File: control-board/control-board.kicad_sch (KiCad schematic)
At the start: 85 parts, among them J1 Conn_01x03, J10 DIN-4, J11 DIN-4, J2 GPS_ANT, J3 LORA_ANT, J4 DIN-4, J5 DIN-4, J6 USB_C_Receptacle_USB2.0_16P, J7 DIN-4, J8 DIN-4, J9 DIN-4, Q1 2N7002, SW1 SW_SPST, U1 STM32H743VITx, U2 NEO-XM, U3 SN65HVD256D, U4 AMS1117-3.3, U5 AP63200WU, U6 AMS1117-3.3, U7 SN65HVD256D, Y1 8M, Y2 32.768k

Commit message: control-board: update Ver 2025.9-1
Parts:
- added D3, D4, D5, D6: LED, LED_SMD:LED_0805_2012Metric, symbol Device:LED
- added H1, H2, H3, H4: MountingHole_Pad, MountingHole:MountingHole_3.2mm_M3_ISO14580_Pad, symbol Mechanical:MountingHole_Pad
- added J12, J13: Conn_01x03, Connector_PinHeader_2.54mm:PinHeader_1x03_P2.54mm_Vertical, symbol Connector_Generic:Conn_01x03
- J10, J11, J4, J5, J7, J8, J9: footprint (none) -> M8_conn_panel:M8_Female_Conn_Panel_P4_90
- JP1, JP2: footprint PCM_Jumper_AKL:Jumper_P2.54mm_D1.2mm -> Connector_PinHeader_2.54mm:PinHeader_1x02_P2.54mm_Vertical
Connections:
- net GND: now also D3.1 (K), D4.1 (K), D5.1 (K), D6.1 (K), H1.1, H2.1, H3.1, H4.1; no longer R15.2, R16.2, R17.2, R9.2
- net GPIO1: now reaches U1.57 (PD10)
- net GPIO1: now also J12.1 (Pin_1)
- net GPIO2: now reaches U1.58 (PD11)
- net GPIO2: now also J12.2 (Pin_2)
- net GPIO3: now reaches U1.59 (PD12)
- net GPIO3: now also J12.3 (Pin_3)
- net GPIO4: now reaches U1.60 (PD13)
- net GPIO4: now also J13.1 (Pin_1)
- net GPIO5: now reaches U1.61 (PD14)
- net GPIO5: now also J13.2 (Pin_2)
- net GPIO6: now reaches U1.62 (PD15)
- net GPIO6: now also J13.3 (Pin_3)
- net GPIO7: now reaches U1.83 (PD2)
- net GPIO8: now reaches U1.84 (PD3)
- net GPIO9: now reaches U1.85 (PD4)
- new net: D3.2 (A), R15.2
- new net: D6.2 (A), R9.2
- new net: D4.2 (A), R16.2
- new net: D5.2 (A), R17.2
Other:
- moved on the sheet: R15, R16, R17, R9

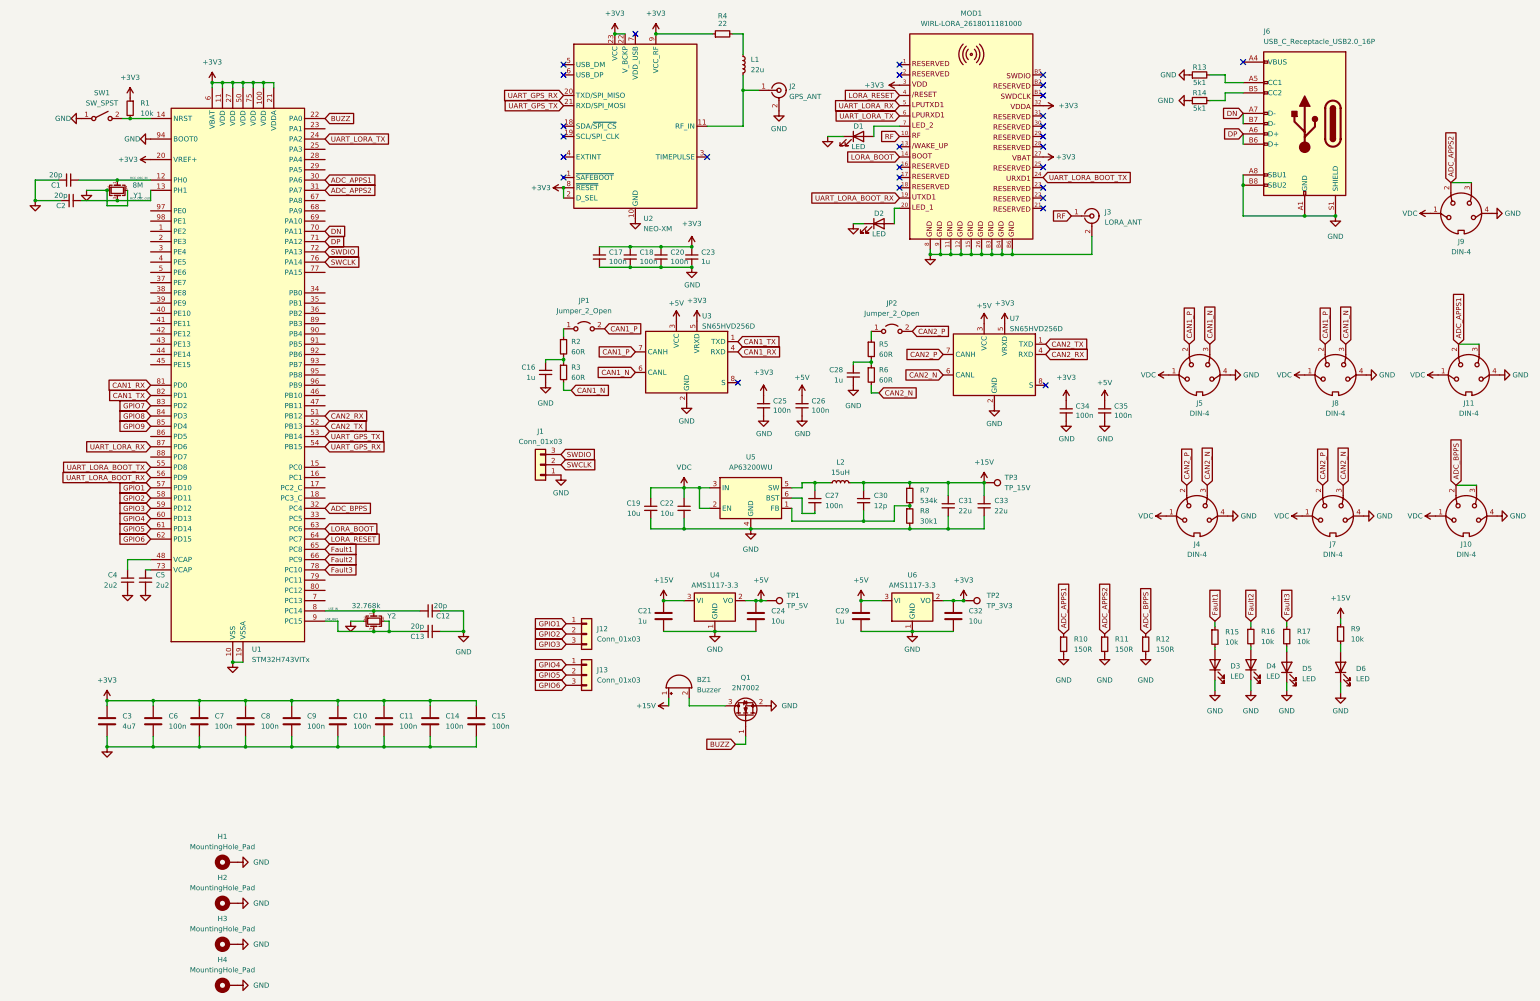
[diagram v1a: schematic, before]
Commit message: modify: control board schematic
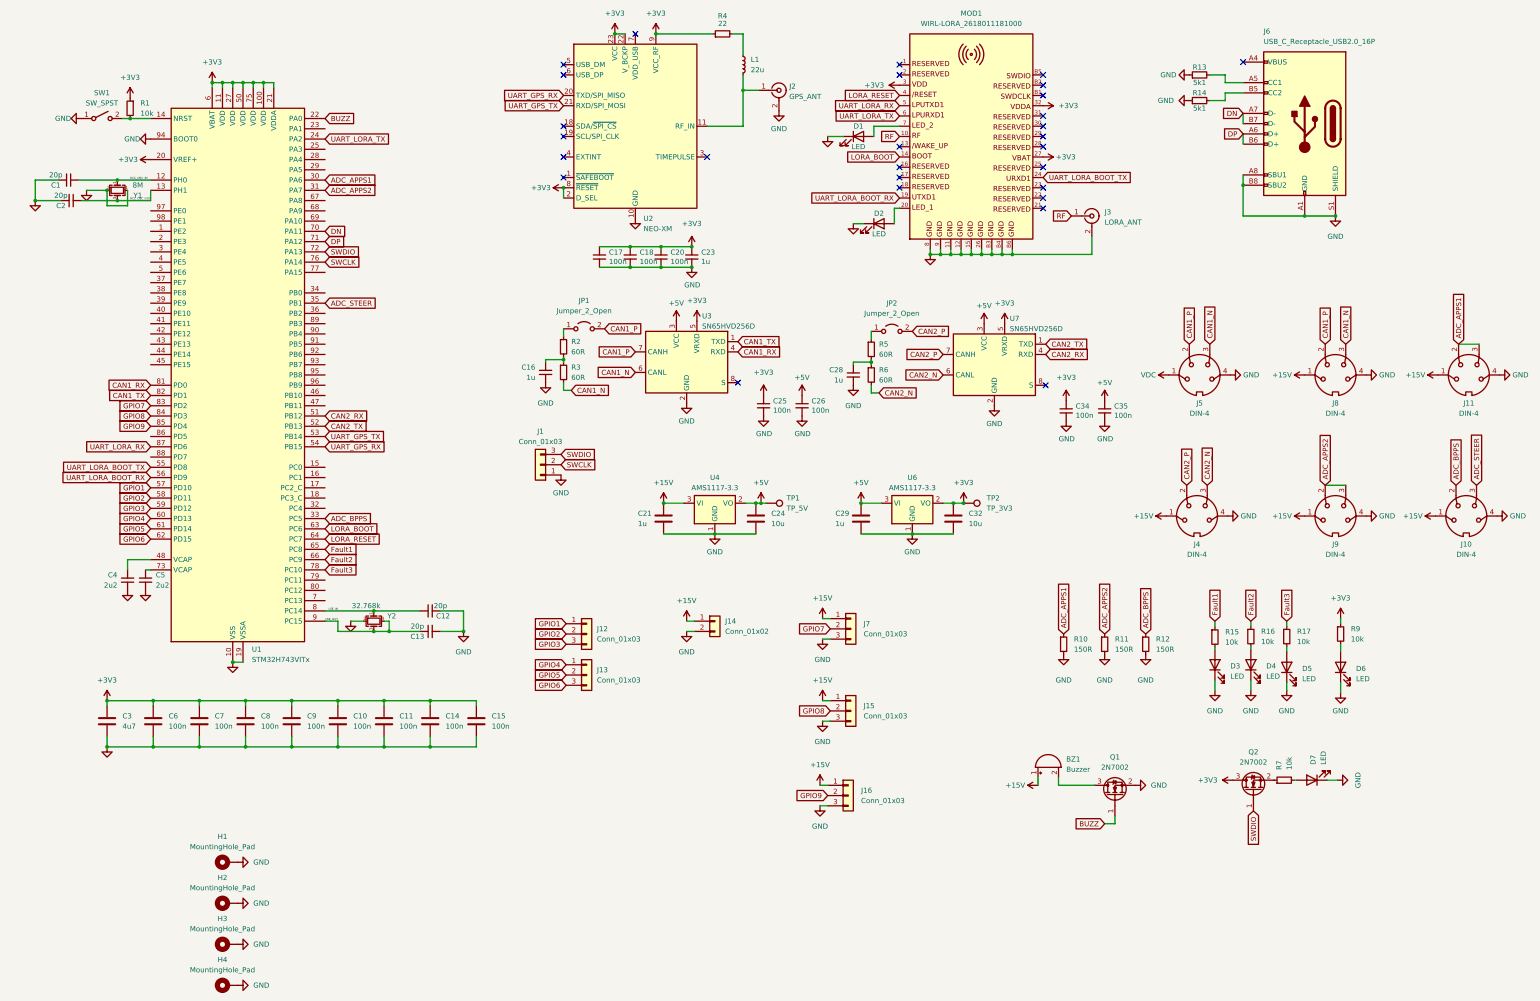
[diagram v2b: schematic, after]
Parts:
- removed C19, C22: 10u, Capacitor_SMD:C_0805_2012Metric, symbol Device:C_Small
- removed C27: 100n, Capacitor_SMD:C_0603_1608Metric, symbol Device:C_Small
- removed C30: 12p, Capacitor_SMD:C_0603_1608Metric, symbol Device:C_Small
- removed C31, C33: 22u, Capacitor_SMD:C_0805_2012Metric, symbol Device:C_Small
- removed J7: DIN-4, M8_conn_panel:M8_Female_Conn_Panel_P4_90, symbol Connector:DIN-4
- removed L2: 15uH, Inductor_SMD:L_Coilcraft_XAL6060-XXX, symbol Device:L_Small
- removed R8: 30k1, Resistor_SMD:R_0603_1608Metric, symbol Device:R_Small
- removed TP3: TP_15V, TestPoint:TestPoint_THTPad_D1.5mm_Drill0.7mm, symbol Connector:TestPoint
- removed U5: AP63200WU, Package_TO_SOT_SMD:TSOT-23-6, symbol Regulator_Switching:AP63200WU
- added D7: LED, LED_SMD:LED_0805_2012Metric, symbol Device:LED
- added J14: Conn_01x02, Connector_PinHeader_2.54mm:PinHeader_1x02_P2.54mm_Vertical, symbol Connector_Generic:Conn_01x02
- added J15, J16, J7: Conn_01x03, symbol Connector_Generic:Conn_01x03
- added Q2: 2N7002, Package_TO_SOT_SMD:SOT-23, symbol Transistor_FET:2N7002
- R7: value 534k -> 10k
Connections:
- net +15V: now also J10.1, J11.1, J4.1, J8.1, J9.1, J14.1 (Pin_1), J15.1 (Pin_1), J16.1 (Pin_1), J7.1 (Pin_1); no longer R7.1, R9.1
- net +3V3: now also R9.1, Q2.3 (D)
- net ADC_BPPS: now also U1.33 (PC5); no longer J10.3, U1.32 (PC4)
- net GND: now also D7.1 (K), J14.2 (Pin_2), J15.3 (Pin_3), J16.3 (Pin_3), J7.3 (Pin_3)
- net GPIO7: now also J7.2 (Pin_2)
- net GPIO8: now also J15.2 (Pin_2)
- net GPIO9: now also J16.2 (Pin_2)
- net SWDIO: now also Q2.1 (G)
- net VDC: no longer J10.1, J11.1, J4.1, J8.1, J9.1
- net at R7.2: now also D7.2 (A)
- net ADC_STEER: now reaches U1.35 (PB1)
- net ADC_STEER: now also J10.3
- new net: Q2.2 (S), R7.1
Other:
- moved on the sheet: BZ1, C21, C24, C29, C32, J9, Q1, TP1, TP2, U4, U6

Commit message: modify: control board
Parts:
- removed J16: Conn_01x03, symbol Connector_Generic:Conn_01x03
- added D8: BAT46, Diode_THT:D_DO-35_SOD27_P7.62mm_Horizontal, symbol Diode:BAT46
- J15, J7: footprint (none) -> Connector_JST:JST_EH_B3B-EH-A_1x03_P2.50mm_Vertical
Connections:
- net +15V: no longer J8.1
- net +3V3: now also R7.1; no longer Q2.3 (D)
- net +5V: now also D8.1 (K)
- net GND: now also Q2.2 (S); no longer D7.1 (K)
- net VDC: now also J8.1
- net at J6.A4 (VBUS), J6.A9 (VBUS), J6.B4 (VBUS)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: now also D8.2 (A)
- net GPIO9: no longer names the net of U1.85 (PD4)
- new net: D7.1 (K), Q2.3 (D)
- no-connect marks 28 -> 27
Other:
- moved on the sheet: D7, Q2, R13, R14, R7

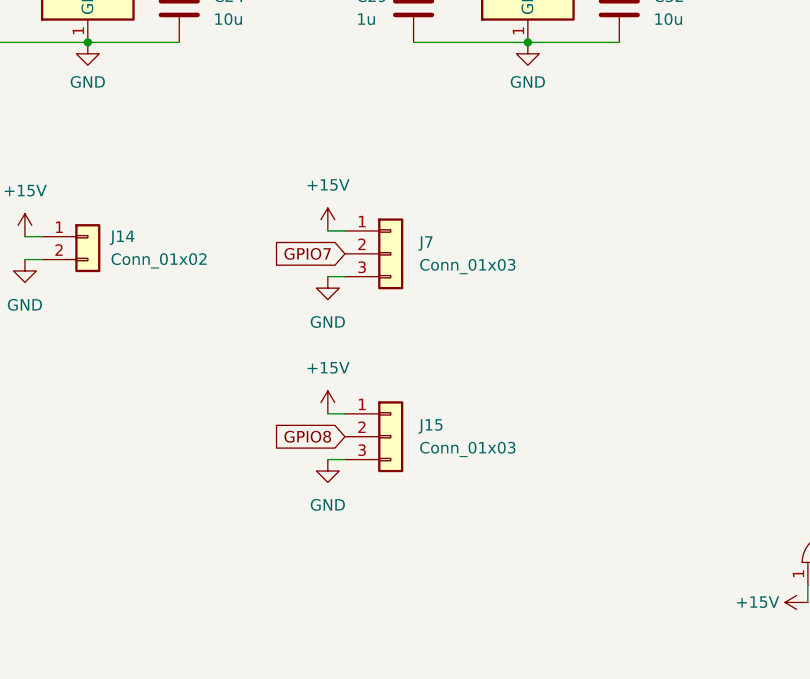
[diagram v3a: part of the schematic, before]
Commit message: modify: diodes and JST footprint
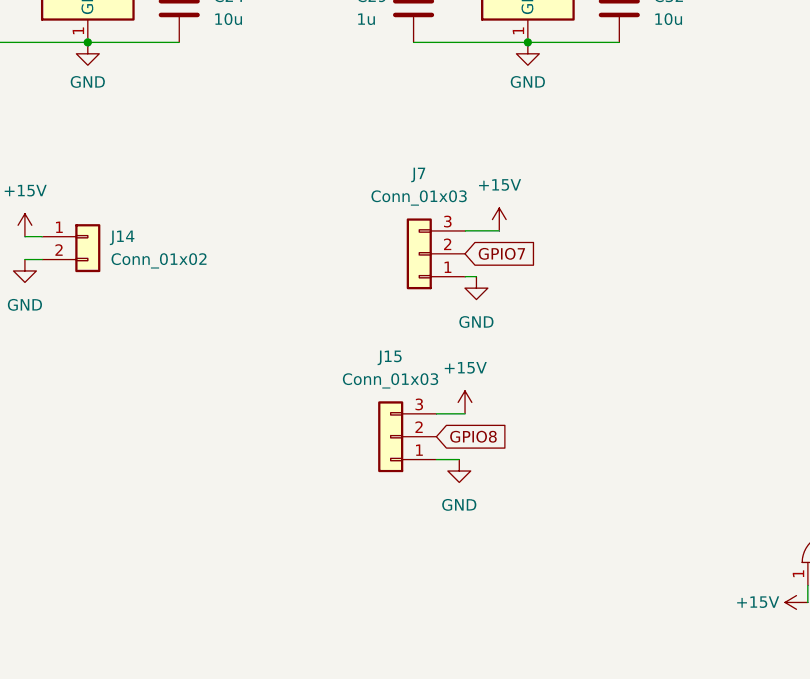
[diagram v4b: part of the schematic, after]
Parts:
- D8: footprint Diode_THT:D_DO-35_SOD27_P7.62mm_Horizontal -> Diode_SMD:D_SOD-123
- J15, J7: footprint Connector_JST:JST_EH_B3B-EH-A_1x03_P2.50mm_Vertical -> Connector_JST:JST_XH_B3B-XH-A_1x03_P2.50mm_Vertical
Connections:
- net +15V: now also J15.3 (Pin_3), J7.3 (Pin_3); no longer J15.1 (Pin_1), J7.1 (Pin_1)
- net GND: now also J15.1 (Pin_1), J7.1 (Pin_1); no longer J15.3 (Pin_3), J7.3 (Pin_3)
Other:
- moved on the sheet: J15, J7
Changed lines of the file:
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@@
     (stroke (width 0) (type default))
   )
+  (wire (pts (xy 241.935 171.45) (xy 240.665 171.45))
+    (stroke (width 0) (type default))
+  )
   (wire (pts (xy 48.26 186.69) (xy 59.69 186.69))
     (stroke (width 0) (type default))
@@
     (stroke (width 0) (type default))
   )
+  (wire (pts (xy 237.49 186.69) (xy 240.665 186.69))
+    (stroke (width 0) (type default))
+  )
   (wire (pts (xy 283.845 205.74) (xy 283.845 207.645))
     (stroke (width 0) (type default))
@@
     (stroke (width 0) (type default))
   )
-  (wire (pts (xy 225.425 191.77) (xy 227.33 191.77))
-    (stroke (width 0) (type default))
-  )
   (wire (pts (xy 53.34 60.325) (xy 53.34 64.135))
     (stroke (width 0) (type default))
@@
     (stroke (width 0) (type default))
   )
-  (wire (pts (xy 225.425 186.69) (xy 227.33 186.69))
-    (stroke (width 0) (type default))
-  )
   (wire (pts (xy 234.95 145.415) (xy 247.65 145.415))
     (stroke (width 0) (type default))
@@
     (stroke (width 0) (type default))
   )
+  (wire (pts (xy 240.03 191.77) (xy 237.49 191.77))
+    (stroke (width 0) (type default))
+  )
   (wire (pts (xy 292.1 76.2) (xy 292.1 71.755))
     (stroke (width 0) (type default))
@@
     (stroke (width 0) (type default))
   )
-  (wire (pts (xy 225.425 171.45) (xy 227.33 171.45))
-    (stroke (width 0) (type default))
-  )
   (wire (pts (xy 272.415 76.2) (xy 292.1 76.2))
     (stroke (width 0) (type default))
@@
     (stroke (width 0) (type default))
   )
-  (wire (pts (xy 82.55 198.12) (xy 93.98 198.12))
+  (wire (pts (xy 244.475 166.37) (xy 240.665 166.37))
     (stroke (width 0) (type default))
   )
-  (wire (pts (xy 30.48 62.865) (xy 30.48 57.785))
+  (wire (pts (xy 82.55 198.12) (xy 93.98 198.12))
     (stroke (width 0) (type default))
   )
-  (wire (pts (xy 225.425 166.37) (xy 227.33 166.37))
+  (wire (pts (xy 30.48 62.865) (xy 30.48 57.785))
     (stroke (width 0) (type default))
   )
@@
     )
   )
-  (global_label "GPIO8" (shape input) (at 227.33 189.23 180) (fields_autoplaced)
-    (effects (font (size 1.27 1.27)) (justify right))
-    (property "Intersheetrefs" "${INTERSHEET_REFS}" (at 218.66 189.23 0)
-      (effects (font (size 1.27 1.27)) (justify right) hide)
+  (global_label "GPIO8" (shape input) (at 237.49 189.23 0) (fields_autoplaced)
+    (effects (font (size 1.27 1.27)) (justify left))
+    (property "Intersheetrefs" "${INTERSHEET_REFS}" (at 246.16 189.23 0)
+      (effects (font (size 1.27 1.27)) (justify left) hide)
     )
   )
@@
     )
   )
-  (global_label "GPIO7" (shape input) (at 227.33 168.91 180) (fields_autoplaced)
-    (effects (font (size 1.27 1.27)) (justify right))
-    (property "Intersheetrefs" "${INTERSHEET_REFS}" (at 218.66 168.91 0)
-      (effects (font (size 1.27 1.27)) (justify right) hide)
+  (global_label "GPIO7" (shape input) (at 240.665 168.91 0) (fields_autoplaced)
+    (effects (font (size 1.27 1.27)) (justify left))
+    (property "Intersheetrefs" "${INTERSHEET_REFS}" (at 249.335 168.91 0)
+      (effects (font (size 1.27 1.27)) (justify left) hide)
     )
   )
@@
       (effects (font (size 1.27 1.27)))
     )
-    (property "Footprint" "Diode_THT:D_DO-35_SOD27_P7.62mm_Horizontal" (at 325.755 33.02 0)
+    (property "Footprint" "Diode_SMD:D_SOD-123" (at 325.755 33.02 0)
       (effects (font (size 1.27 1.27)) hide)
     )
@@
     )
   )
-  (symbol (lib_id "Connector_Generic:Conn_01x03") (at 232.41 168.91 0) (unit 1)
+  (symbol (lib_id "Connector_Generic:Conn_01x03") (at 235.585 168.91 180) (unit 1)
     (in_bom yes) (on_board yes) (dnp no) (fields_autoplaced)
-    (property "Reference" "J7" (at 235.585 167.64 0)
-      (effects (font (size 1.27 1.27)) (justify left))
+    (property "Reference" "J7" (at 235.585 160.02 0)
+      (effects (font (size 1.27 1.27)))
     )
-    (property "Value" "Conn_01x03" (at 235.585 170.18 0)
-      (effects (font (size 1.27 1.27)) (justify left))
+    (property "Value" "Conn_01x03" (at 235.585 162.56 0)
+      (effects (font (size 1.27 1.27)))
     )
-    (property "Footprint" "Connector_JST:JST_EH_B3B-EH-A_1x03_P2.50mm_Vertical" (at 232.41 168.91 0)
+    (property "Footprint" "Connector_JST:JST_XH_B3B-XH-A_1x03_P2.50mm_Vertical" (at 235.585 168.91 0)
       (effects (font (size 1.27 1.27)) hide)
     )
-    (property "Datasheet" "~" (at 232.41 168.91 0)
+    (property "Datasheet" "~" (at 235.585 168.91 0)
       (effects (font (size 1.27 1.27)) hide)
     )
@@
     )
   )
-  (symbol (lib_id "power:GND") (at 225.425 171.45 0) (unit 1)
+  (symbol (lib_id "power:GND") (at 241.935 171.45 0) (unit 1)
     (in_bom yes) (on_board yes) (dnp no) (fields_autoplaced)
-    (property "Reference" "#PWR085" (at 225.425 177.8 0)
+    (property "Reference" "#PWR085" (at 241.935 177.8 0)
       (effects (font (size 1.27 1.27)) hide)
     )
-    (property "Value" "GND" (at 225.425 176.53 0)
+    (property "Value" "GND" (at 241.935 176.53 0)
       (effects (font (size 1.27 1.27)))
     )
-    (property "Footprint" "" (at 225.425 171.45 0)
+    (property "Footprint" "" (at 241.935 171.45 0)
       (effects (font (size 1.27 1.27)) hide)
     )
-    (property "Datasheet" "" (at 225.425 171.45 0)
+    (property "Datasheet" "" (at 241.935 171.45 0)
       (effects (font (size 1.27 1.27)) hide)
     )
@@
     )
   )
-  (symbol (lib_id "power:+15V") (at 225.425 186.69 0) (unit 1)
-    (in_bom yes) (on_board yes) (dnp no) (fields_autoplaced)
-    (property "Reference" "#PWR086" (at 225.425 190.5 0)
+  (symbol (lib_id "power:+15V") (at 240.665 186.69 0) (mirror y) (unit 1)
+    (in_bom yes) (on_board yes) (dnp no)
+    (property "Reference" "#PWR086" (at 240.665 190.5 0)
       (effects (font (size 1.27 1.27)) hide)
     )
-    (property "Value" "+15V" (at 225.425 181.61 0)
+    (property "Value" "+15V" (at 240.665 181.61 0)
       (effects (font (size 1.27 1.27)))
     )
-    (property "Footprint" "" (at 225.425 186.69 0)
+    (property "Footprint" "" (at 240.665 186.69 0)
       (effects (font (size 1.27 1.27)) hide)
     )
-    (property "Datasheet" "" (at 225.425 186.69 0)
+    (property "Datasheet" "" (at 240.665 186.69 0)
       (effects (font (size 1.27 1.27)) hide)
     )
@@
     )
   )
-  (symbol (lib_id "power:GND") (at 225.425 191.77 0) (unit 1)
+  (symbol (lib_id "power:GND") (at 240.03 191.77 0) (unit 1)
     (in_bom yes) (on_board yes) (dnp no) (fields_autoplaced)
-    (property "Reference" "#PWR087" (at 225.425 198.12 0)
+    (property "Reference" "#PWR087" (at 240.03 198.12 0)
       (effects (font (size 1.27 1.27)) hide)
     )
-    (property "Value" "GND" (at 225.425 196.85 0)
+    (property "Value" "GND" (at 240.03 196.85 0)
       (effects (font (size 1.27 1.27)))
     )
-    (property "Footprint" "" (at 225.425 191.77 0)
+    (property "Footprint" "" (at 240.03 191.77 0)
       (effects (font (size 1.27 1.27)) hide)
     )
-    (property "Datasheet" "" (at 225.425 191.77 0)
+    (property "Datasheet" "" (at 240.03 191.77 0)
       (effects (font (size 1.27 1.27)) hide)
     )
@@
     )
   )
-  (symbol (lib_id "Connector_Generic:Conn_01x03") (at 232.41 189.23 0) (unit 1)
+  (symbol (lib_id "Connector_Generic:Conn_01x03") (at 232.41 189.23 180) (unit 1)
     (in_bom yes) (on_board yes) (dnp no) (fields_autoplaced)
-    (property "Reference" "J15" (at 235.585 187.96 0)
-      (effects (font (size 1.27 1.27)) (justify left))
+    (property "Reference" "J15" (at 232.41 180.34 0)
+      (effects (font (size 1.27 1.27)))
     )
-    (property "Value" "Conn_01x03" (at 235.585 190.5 0)
-      (effects (font (size 1.27 1.27)) (justify left))
+    (property "Value" "Conn_01x03" (at 232.41 182.88 0)
+      (effects (font (size 1.27 1.27)))
     )
-    (property "Footprint" "Connector_JST:JST_EH_B3B-EH-A_1x03_P2.50mm_Vertical" (at 232.41 189.23 0)
+    (property "Footprint" "Connector_JST:JST_XH_B3B-XH-A_1x03_P2.50mm_Vertical" (at 232.41 189.23 0)
       (effects (font (size 1.27 1.27)) hide)
     )
@@
     )
   )
-  (symbol (lib_id "power:+15V") (at 225.425 166.37 0) (unit 1)
+  (symbol (lib_id "power:+15V") (at 244.475 166.37 0) (unit 1)
     (in_bom yes) (on_board yes) (dnp no) (fields_autoplaced)
-    (property "Reference" "#PWR073" (at 225.425 170.18 0)
+    (property "Reference" "#PWR073" (at 244.475 170.18 0)
       (effects (font (size 1.27 1.27)) hide)
     )
-    (property "Value" "+15V" (at 225.425 161.29 0)
+    (property "Value" "+15V" (at 244.475 161.29 0)
       (effects (font (size 1.27 1.27)))
     )
-    (property "Footprint" "" (at 225.425 166.37 0)
+    (property "Footprint" "" (at 244.475 166.37 0)
       (effects (font (size 1.27 1.27)) hide)
     )
-    (property "Datasheet" "" (at 225.425 166.37 0)
+    (property "Datasheet" "" (at 244.475 166.37 0)
       (effects (font (size 1.27 1.27)) hide)
     )
